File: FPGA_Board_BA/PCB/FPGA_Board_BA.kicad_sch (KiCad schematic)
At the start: 4 parts

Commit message: lots of work
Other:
- note added: "- DCDC for Differential-amplifier [X] ADC power supply (1.8V ... 2.5V) - Breakout for all unused pins - ESD Diode Array for unused pins [X] Add another ADC for B6 [X] CHB Rx En Err -> 10 pin (wie base board) - Poti an Analog Input - ADC Datenbatt Recherche LVDS/CMOS ob 24pin + 2pins für comversion start frei sind [X] FPGA falsche pin namen an Hersteller + BA [X] Level shifter für Tx Rx und Fault 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"
- note removed: "- DCDC for Differential-amplifier [X] ADC power supply (1.8V ... 2.5V) - Breakout for all unused pins - ESD Diode Array for unused pins [X] Add another ADC for B6 - CHB Rx En Err -> 10 pin (wie base board) - Poti an Analog Input - ADC Datenbatt Recherche LVDS/CMOS ob 24pin + 2pins für comversion start frei sind [X] FPGA falsche pin namen an Hersteller + BA - Level shifter für Tx Rx und Fault pins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"
- moved on the sheet: R1, R101, R2, R3

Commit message: work
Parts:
- renumbered R101 to R4
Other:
- sheet ADC for B6 ports: added CNV; removed ~{CNV}
- sheet ADC for Machine ports: added CNV_1; removed ~{CNV}_1
- sheet FPGA ports: added CNV, CNV_1; removed ~{CNV}, ~{CNV}_1
- note added: "- DCDC for Differential-amplifier [X] ADC power supply (1.8V ... 2.5V) - Breakout for all unused pins - ESD Diode Array for unused pins [X] Add another ADC for B6 [X] CHB Rx En Err -> 10 pin (wie base board) [X] Poti an Analog Input - ADC Datenbatt Recherche LVDS/CMOS ob 24pin + 2pins für comversion start frei sind [X] FPGA falsche pin namen an Hersteller + BA [X] Level shifter für Tx Rx und Faul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"
- note removed: "- DCDC for Differential-amplifier [X] ADC power supply (1.8V ... 2.5V) - Breakout for all unused pins - ESD Diode Array for unused pins [X] Add another ADC for B6 [X] CHB Rx En Err -> 10 pin (wie base board) - Poti an Analog Input - ADC Datenbatt Recherche LVDS/CMOS ob 24pin + 2pins für comversion start frei sind [X] FPGA falsche pin namen an Hersteller + BA [X] Level shifter für Tx Rx und Fault 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"
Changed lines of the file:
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@@
 	(generator_version "9.0")
 	(paper "A3")
-	(text "- DCDC for Differential-amplifier\n[X] ADC power supply (1.8V ... 2.5V)\n- Breakout for all unused pins\n- ESD Diode Array for unused pins\n[X] Add another ADC for B6\n[X] CHB Rx En Err -> 10 pin (wie base board)\n- Poti an Analog Input\n- ADC Datenbatt Recherche LVDS/CMOS ob 24pin + 2pins für comversion start frei sind\n[X] FPGA falsche pin namen an Hersteller + BA \n[X] Level shifter für Tx Rx und Fault pins (CHB -> FPGA)\n- Pullup Resistor für Tx der CHB und auch Rx\n[X] Latex dokumentation beginnen\n[X] Diff Eingang für ADC (mit OP-Amps)\n[X] CMOS Fest, DDR mit 2 Widerstände\n[X] HV-Probe hinzufügen\n[X] 26 pin wannenstecker\n- RapidHarness Verkabelung"
+	(text "- DCDC for Differential-amplifier\n[X] ADC power supply (1.8V ... 2.5V)\n- Breakout for all unused pins\n- ESD Diode Array for unused pins\n[X] Add another ADC for B6\n[X] CHB Rx En Err -> 10 pin (wie base board)\n[X] Poti an Analog Input\n- ADC Datenbatt Recherche LVDS/CMOS ob 24pin + 2pins für comversion start frei sind\n[X] FPGA falsche pin namen an Hersteller + BA \n[X] Level shifter für Tx Rx und Fault pins (CHB -> FPGA)\n[X] Pullup Resistor für Tx der CHB und auch Rx\n[X] Latex dokumentation beginnen\n[X] Diff Eingang für ADC (mit OP-Amps)\n[X] CMOS Fest, DDR mit 2 Widerstände\n[X] HV-Probe hinzufügen\n[X] 26 pin wannenstecker\n- RapidHarness Verkabelung\n- 0402 R und C\n- CHB to PCB connect gleich wie beim Base-Board"
 		(exclude_from_sim no)
 		(at 302.26 230.378 0)
@@
 	(wire
 		(pts
-			(xy 115.57 62.23) (xy 156.21 62.23)
+			(xy 115.57 73.66) (xy 156.21 73.66)
 		)
 		(stroke
@@
 	(wire
 		(pts
-			(xy 198.12 72.39) (xy 222.25 72.39)
+			(xy 198.12 95.25) (xy 222.25 95.25)
 		)
 		(stroke
@@
 	(wire
 		(pts
-			(xy 198.12 86.36) (xy 222.25 86.36)
+			(xy 198.12 109.22) (xy 222.25 109.22)
 		)
 		(stroke
@@
 	(wire
 		(pts
-			(xy 115.57 67.31) (xy 156.21 67.31)
+			(xy 115.57 78.74) (xy 156.21 78.74)
 		)
 		(stroke
@@
 	(wire
 		(pts
-			(xy 198.12 67.31) (xy 222.25 67.31)
+			(xy 198.12 90.17) (xy 222.25 90.17)
 		)
 		(stroke
@@
 	(wire
 		(pts
-			(xy 198.12 81.28) (xy 222.25 81.28)
+			(xy 198.12 104.14) (xy 222.25 104.14)
 		)
 		(stroke
@@
 	(wire
 		(pts
-			(xy 198.12 78.74) (xy 222.25 78.74)
+			(xy 198.12 101.6) (xy 222.25 101.6)
 		)
 		(stroke
@@
 	(wire
 		(pts
-			(xy 198.12 96.52) (xy 222.25 96.52)
+			(xy 198.12 119.38) (xy 222.25 119.38)
 		)
 		(stroke
@@
 	(wire
 		(pts
-			(xy 198.12 88.9) (xy 222.25 88.9)
+			(xy 198.12 111.76) (xy 222.25 111.76)
 		)
 		(stroke
@@
 	(wire
 		(pts
-			(xy 115.57 72.39) (xy 156.21 72.39)
+			(xy 115.57 83.82) (xy 156.21 83.82)
 		)
 		(stroke
@@
 	(wire
 		(pts
-			(xy 198.12 91.44) (xy 222.25 91.44)
+			(xy 198.12 114.3) (xy 222.25 114.3)
 		)
 		(stroke
@@
 	(wire
 		(pts
-			(xy 198.12 83.82) (xy 222.25 83.82)
+			(xy 198.12 106.68) (xy 222.25 106.68)
 		)
 		(stroke
@@
 	(wire
 		(pts
-			(xy 198.12 69.85) (xy 222.25 69.85)
+			(xy 198.12 92.71) (xy 222.25 92.71)
 		)
 		(stroke
@@
 	(wire
 		(pts
-			(xy 198.12 93.98) (xy 222.25 93.98)
+			(xy 198.12 116.84) (xy 222.25 116.84)
 		)
 		(stroke
@@
 	(wire
 		(pts
-			(xy 115.57 64.77) (xy 156.21 64.77)
+			(xy 115.57 76.2) (xy 156.21 76.2)
 		)
 		(stroke
@@
 	(wire
 		(pts
-			(xy 115.57 69.85) (xy 156.21 69.85)
+			(xy 115.57 81.28) (xy 156.21 81.28)
 		)
 		(stroke
@@
 		(on_board yes)
 		(dnp no)
-		(property "Reference" "R101"
+		(property "Reference" "R4"
 			(at 360.426 80.518 90)
 			(effects
@@
 			(project "FPGA_Board_BA"
 				(path "/fd7503bc-e7fc-4766-b224-3d1c3d7de5ff"
-					(reference "R101")
+					(reference "R4")
 					(unit 1)
 				)
@@
 	)
 	(sheet
-		(at 90.17 59.69)
+		(at 90.17 71.12)
 		(size 25.4 15.24)
 		(exclude_from_sim no)
@@
 		)
 		(property "Sheetname" "User Interaction"
-			(at 90.17 58.9784 0)
+			(at 90.17 70.4084 0)
 			(effects
 				(font
@@
 		)
 		(property "Sheetfile" "user_interaction.kicad_sch"
-			(at 90.17 75.5146 0)
+			(at 90.17 86.9446 0)
 			(effects
 				(font
@@
 		)
 		(pin "Button1" output
-			(at 115.57 62.23 0)
+			(at 115.57 73.66 0)
 			(effects
 				(font
@@
 		)
 		(pin "Button2" output
-			(at 115.57 64.77 0)
+			(at 115.57 76.2 0)
 			(effects
 				(font
@@
 		)
 		(pin "LED1" input
-			(at 115.57 67.31 0)
+			(at 115.57 78.74 0)
 			(effects
 				(font
@@
 		)
 		(pin "LED2" input
-			(at 115.57 69.85 0)
+			(at 115.57 81.28 0)
 			(effects
 				(font
@@
 		)
 		(pin "Poti" output
-			(at 115.57 72.39 0)
+			(at 115.57 83.82 0)
 			(effects
 				(font
@@
 	)
 	(sheet
-		(at 222.25 59.69)
-		(size 34.29 83.82)
+		(at 222.25 69.85)
+		(size 34.29 73.66)
 		(exclude_from_sim no)
 		(in_bom yes)
@@
 		)
 		(property "Sheetname" "ADC for Machine"
-			(at 222.25 58.9784 0)
+			(at 222.25 69.1384 0)
 			(effects
 				(font
@@
 		)
 		(pin "CLK_IN_1" input
-			(at 222.25 67.31 180)
+			(at 222.25 90.17 180)
 			(effects
 				(font
@@
 		)
 		(pin "CLK_OUT_1" input
-			(at 222.25 69.85 180)
+			(at 222.25 92.71 180)
 			(effects
 				(font
@@
 		)
 		(pin "SDO1_1" output
-			(at 222.25 78.74 180)
+			(at 222.25 101.6 180)
 			(effects
 				(font
@@
 		)
 		(pin "SDO2_1" output
-			(at 222.25 81.28 180)
+			(at 222.25 104.14 180)
 			(effects
 				(font
@@
 		)
 		(pin "SDO3_1" output
-			(at 222.25 83.82 180)
+			(at 222.25 106.68 180)
 			(effects
 				(font
@@
 		)
 		(pin "SDO4_1" output
-			(at 222.25 86.36 180)
+			(at 222.25 109.22 180)
 			(effects
 				(font
@@
 		)
 		(pin "SDO5_1" output
-			(at 222.25 88.9 180)
+			(at 222.25 111.76 180)
 			(effects
 				(font
@@
 		)
 		(pin "SDO6_1" output
-			(at 222.25 91.44 180)
+			(at 222.25 114.3 180)
 			(effects
 				(font
@@
 		)
 		(pin "SDO7_1" output
-			(at 222.25 93.98 180)
+			(at 222.25 116.84 180)
 			(effects
 				(font
@@
 		)
 		(pin "SDO8_1" output
-			(at 222.25 96.52 180)
+			(at 222.25 119.38 180)
 			(effects
 				(font
@@
 			)
 		)
-		(pin "~{CNV}_1" input
-			(at 222.25 72.39 180)
+		(pin "CNV_1" input
+			(at 222.25 95.25 180)
 			(effects
 				(font
@@
 	)
 	(sheet
-		(at 156.21 58.42)
-		(size 41.91 220.98)
+		(at 156.21 64.77)
+		(size 41.91 214.63)
 		(exclude_from_sim no)
 		(in_bom yes)
@@
 		)
 		(property "Sheetname" "FPGA"
-			(at 156.21 57.7084 0)
+			(at 156.21 64.0584 0)
 			(effects
 				(font
@@
 			)
 		)
-		(pin "~{CNV}" output
-			(at 198.12 180.34 0)
-			(effects
-				(font
-					(size 1.27 1.27)
-				)
-				(justify right)
-			)
-		)
 		(pin "Ph_C_Tx1" input
 			(at 156.21 181.61 180)
@@
 		)
 		(pin "Button1" input
-			(at 156.21 62.23 180)
+			(at 156.21 73.66 180)
 			(effects
 				(font
@@
 		)
 		(pin "Button2" input
-			(at 156.21 64.77 180)
+			(at 156.21 76.2 180)
 			(effects
 				(font
@@
 		)
 		(pin "LED1" output
-			(at 156.21 67.31 180)
+			(at 156.21 78.74 180)
 			(effects
 				(font
@@
 		)
 		(pin "LED2" output
-			(at 156.21 69.85 180)
+			(at 156.21 81.28 180)
 			(effects
 				(font
@@
 		)
 		(pin "Poti" input
-			(at 156.21 72.39 180)
+			(at 156.21 83.82 180)
 			(effects
 				(font
@@
 		)
 		(pin "CLK_IN_1" output
-			(at 198.12 67.31 0)
+			(at 198.12 90.17 0)
 			(effects
 				(font
@@
 		)
 		(pin "CLK_OUT_1" output
-			(at 198.12 69.85 0)
+			(at 198.12 92.71 0)
 			(effects
 				(font
@@
 		)
 		(pin "SDO1_1" input
-			(at 198.12 78.74 0)
+			(at 198.12 101.6 0)
 			(effects
 				(font
@@
 		)
 		(pin "SDO2_1" input
-			(at 198.12 81.28 0)
+			(at 198.12 104.14 0)
 			(effects
 				(font
@@
 		)
 		(pin "SDO3_1" input
-			(at 198.12 83.82 0)
+			(at 198.12 106.68 0)
 			(effects
 				(font
@@
 		)
 		(pin "SDO4_1" input
-			(at 198.12 86.36 0)
+			(at 198.12 109.22 0)
 			(effects
 				(font
@@
 		)
 		(pin "SDO5_1" input
-			(at 198.12 88.9 0)
+			(at 198.12 111.76 0)
 			(effects
 				(font
@@
 		)
 		(pin "SDO6_1" input
-			(at 198.12 91.44 0)
+			(at 198.12 114.3 0)
 			(effects
 				(font
@@
 		)
 		(pin "SDO7_1" input
-			(at 198.12 93.98 0)
+			(at 198.12 116.84 0)
 			(effects
 				(font
@@
 		)
 		(pin "SDO8_1" input
-			(at 198.12 96.52 0)
+			(at 198.12 119.38 0)
 			(effects
 				(font
@@
 			)
 		)
-		(pin "~{CNV}_1" output
-			(at 198.12 72.39 0)
+		(pin "CNV_1" output
+			(at 198.12 95.25 0)
+			(effects
+				(font
+					(size 1.27 1.27)
+				)
+				(justify right)
+			)
+		)
+		(pin "CNV" output
+			(at 198.12 180.34 0)
 			(effects
 				(font
@@
 			)
 		)
-		(pin "~{CNV}" input
-			(at 223.52 180.34 180)
-			(effects
-				(font
-					(size 1.27 1.27)
-				)
-				(justify left)
-			)
-		)
 		(pin "I_A" input
 			(at 232.41 213.36 270)
@@
 			(effects
 				(font
+					(size 1.27 1.27)
+				)
+				(justify left)
+			)
+		)
+		(pin "CNV" input
+			(at 223.52 180.34 180)
+			(effects
+				(font

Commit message: 18.11 Bib Session
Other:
- sheet ADC for B6 ports: added ~{CNV}; removed CNV
- sheet ADC for Machine ports: added ~{CNV}_1; removed CNV_1
- sheet FPGA ports: added ~{CNV}, ~{CNV}_1; removed CNV, CNV_1
- note added: "- DCDC for Isolation-amplifier [X] ADC power supply (1.8V ... 2.5V) - Breakout for all unused pins - ESD Diode Array for unused pins [X] Add another ADC for B6 [X] CHB Rx En Err -> 10 pin (wie base board) [X] Poti an Analog Input [X] ADC Datenbatt Recherche LVDS/CMOS ob 24pin + 2pins für comversion start frei sind [X] FPGA falsche pin namen an Hersteller + BA [X] Level shifter für Tx Rx und Fault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"
- note removed: "- DCDC for Differential-amplifier [X] ADC power supply (1.8V ... 2.5V) - Breakout for all unused pins - ESD Diode Array for unused pins [X] Add another ADC for B6 [X] CHB Rx En Err -> 10 pin (wie base board) [X] Poti an Analog Input - ADC Datenbatt Recherche LVDS/CMOS ob 24pin + 2pins für comversion start frei sind [X] FPGA falsche pin namen an Hersteller + BA [X] Level shifter für Tx Rx und Faul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"
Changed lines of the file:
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@@
 	(generator_version "9.0")
 	(paper "A3")
-	(text "- DCDC for Differential-amplifier\n[X] ADC power supply (1.8V ... 2.5V)\n- Breakout for all unused pins\n- ESD Diode Array for unused pins\n[X] Add another ADC for B6\n[X] CHB Rx En Err -> 10 pin (wie base board)\n[X] Poti an Analog Input\n- ADC Datenbatt Recherche LVDS/CMOS ob 24pin + 2pins für comversion start frei sind\n[X] FPGA falsche pin namen an Hersteller + BA \n[X] Level shifter für Tx Rx und Fault pins (CHB -> FPGA)\n[X] Pullup Resistor für Tx der CHB und auch Rx\n[X] Latex dokumentation beginnen\n[X] Diff Eingang für ADC (mit OP-Amps)\n[X] CMOS Fest, DDR mit 2 Widerstände\n[X] HV-Probe hinzufügen\n[X] 26 pin wannenstecker\n- RapidHarness Verkabelung\n- 0402 R und C\n- CHB to PCB connect gleich wie beim Base-Board"
+	(text "- DCDC for Isolation-amplifier\n[X] ADC power supply (1.8V ... 2.5V)\n- Breakout for all unused pins\n- ESD Diode Array for unused pins\n[X] Add another ADC for B6\n[X] CHB Rx En Err -> 10 pin (wie base board)\n[X] Poti an Analog Input\n[X] ADC Datenbatt Recherche LVDS/CMOS ob 24pin + 2pins für comversion start frei sind\n[X] FPGA falsche pin namen an Hersteller + BA \n[X] Level shifter für Tx Rx und Fault pins (CHB -> FPGA)\n[X] Pullup Resistor für Tx der CHB und auch Rx\n[X] Latex dokumentation beginnen\n[X] Diff Eingang für ADC (mit OP-Amps)\n[X] CMOS Fest, DDR mit 2 Widerstände\n[X] HV-Probe hinzufügen\n[X] 26 pin wannenstecker\n- CHB to PCB Connector \n- 0402 R und C (maybe)\n- Plug Terminal 8 Pin Footprint korrigieren\n- Alle unconnected pins mit dem \"not-connected\" funktion machen"
 		(exclude_from_sim no)
 		(at 302.26 230.378 0)
@@
 			)
 		)
-		(pin "CLK_OUT_1" input
-			(at 222.25 92.71 180)
-			(effects
-				(font
-					(size 1.27 1.27)
-				)
-				(justify left)
-			)
-		)
 		(pin "SDO1_1" output
 			(at 222.25 101.6 180)
@@
 			)
 		)
-		(pin "CNV_1" input
-			(at 222.25 95.25 180)
-			(effects
-				(font
-					(size 1.27 1.27)
-				)
-				(justify left)
-			)
-		)
 		(pin "Vout_1" input
 			(at 256.54 121.92 0)
@@
 			)
 		)
+		(pin "CLK_OUT_1" output
+			(at 222.25 92.71 180)
+			(effects
+				(font
+					(size 1.27 1.27)
+				)
+				(justify left)
+			)
+		)
+		(pin "~{CNV}_1" input
+			(at 222.25 95.25 180)
+			(effects
+				(font
+					(size 1.27 1.27)
+				)
+				(justify left)
+			)
+		)
 		(instances
 			(project "FPGA_Board_BA"
@@
 			)
 		)
-		(pin "CLK_OUT" output
-			(at 198.12 177.8 0)
-			(effects
-				(font
-					(size 1.27 1.27)
-				)
-				(justify right)
-			)
-		)
 		(pin "Ph_C_Tx1" input
 			(at 156.21 181.61 180)
@@
 			)
 		)
-		(pin "CLK_OUT_1" output
-			(at 198.12 92.71 0)
-			(effects
-				(font
-					(size 1.27 1.27)
-				)
-				(justify right)
-			)
-		)
 		(pin "SDO1_1" input
 			(at 198.12 101.6 0)
@@
 			)
 		)
-		(pin "CNV_1" output
-			(at 198.12 95.25 0)
+		(pin "CLK_OUT_1" input
+			(at 198.12 92.71 0)
 			(effects
 				(font
@@
 			)
 		)
-		(pin "CNV" output
+		(pin "CLK_OUT" input
+			(at 198.12 177.8 0)
+			(effects
+				(font
+					(size 1.27 1.27)
+				)
+				(justify right)
+			)
+		)
+		(pin "~{CNV}" output
 			(at 198.12 180.34 0)
 			(effects
@@
 			)
 		)
+		(pin "~{CNV}_1" output
+			(at 198.12 95.25 0)
+			(effects
+				(font
+					(size 1.27 1.27)
+				)
+				(justify right)
+			)
+		)
 		(instances
 			(project "FPGA_Board_BA"
@@
 			)
 		)
-		(pin "CLK_OUT" input
-			(at 223.52 177.8 180)
-			(effects
-				(font
-					(size 1.27 1.27)
-				)
-				(justify left)
-			)
-		)
 		(pin "SDO1" output
 			(at 223.52 185.42 180)
@@
 			)
 		)
-		(pin "CNV" input
+		(pin "CLK_OUT" output
+			(at 223.52 177.8 180)
+			(effects
+				(font
+					(size 1.27 1.27)
+				)
+				(justify left)
+			)
+		)
+		(pin "~{CNV}" input
 			(at 223.52 180.34 180)
 			(effects

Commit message: Besprechung mit Leo
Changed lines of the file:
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@@
 	(generator_version "9.0")
 	(paper "A3")
-	(text "- DCDC for Isolation-amplifier\n[X] ADC power supply (1.8V ... 2.5V)\n- Breakout for all unused pins\n- ESD Diode Array for unused pins\n[X] Add another ADC for B6\n[X] CHB Rx En Err -> 10 pin (wie base board)\n[X] Poti an Analog Input\n[X] ADC Datenbatt Recherche LVDS/CMOS ob 24pin + 2pins für comversion start frei sind\n[X] FPGA falsche pin namen an Hersteller + BA \n[X] Level shifter für Tx Rx und Fault pins (CHB -> FPGA)\n[X] Pullup Resistor für Tx der CHB und auch Rx\n[X] Latex dokumentation beginnen\n[X] Diff Eingang für ADC (mit OP-Amps)\n[X] CMOS Fest, DDR mit 2 Widerstände\n[X] HV-Probe hinzufügen\n[X] 26 pin wannenstecker\n- CHB to PCB Connector \n- 0402 R und C (maybe)\n- Plug Terminal 8 Pin Footprint korrigieren\n- Alle unconnected pins mit dem \"not-connected\" funktion machen"
+	(text "- DCDC for Isolation-amplifier\n[X] ADC power supply (1.8V ... 2.5V)\n- Breakout for all unused pins\n- ESD Diode Array for unused pins\n[X] Add another ADC for B6\n[X] CHB Rx En Err -> 10 pin (wie base board)\n[X] Poti an Analog Input\n[X] ADC Datenbatt Recherche LVDS/CMOS ob 24pin + 2pins für comversion start frei sind\n[X] FPGA falsche pin namen an Hersteller + BA \n[X] Level shifter für Tx Rx und Fault pins (CHB -> FPGA)\n[X] Pullup Resistor für Tx der CHB und auch Rx\n[X] Latex dokumentation beginnen\n[X] Diff Eingang für ADC (mit OP-Amps)\n[X] CMOS Fest, DDR mit 2 Widerstände\n[X] HV-Probe hinzufügen\n[X] 26 pin wannenstecker\n- CHB to PCB Connector \n- 0402 R und C (maybe)\n- Plug Terminal 8 Pin Footprint korrigieren\n- Alle unconnected pins mit dem \"not-connected\" funktion machen\n- Drehzahlsensor widerstand zum dir pin von level shifter\n- En Pulldown (wahrscheinlich (muss noch nachschauen))\n- Error auch\n- Rx vor dem Level-Shifter pull-up\n- Leo link schicken über 24 pin Wannenstecker Mouser\n- Noch einen Poti \n- Refout -> 2 Opamps für diff-Eingang (Vref/2)\n- Xilinx pinout anschauen + Versorgung\n- Vllt ein Bank auf 1.8V"
 		(exclude_from_sim no)
-		(at 302.26 230.378 0)
+		(at 278.892 244.348 0)
 		(effects
 			(font

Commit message: 22.11
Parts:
- removed R1, R2, R3, R4: 0R100_2512, Resistor_SMD:R_2512_6332Metric_Pad1.40x3.35mm_HandSolder, symbol MYLIB_R:0R100_2512
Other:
- removed sheet ADC power
- sheet ADC for Machine ports: added Iin_1, Iin_2, Iin_3, Iin_4; removed none
- sheet Current measure ports: added PHA, PHB, PHC, PHD; removed PHA_OUTN, PHA_OUTP, PHB_OUTN, PHB_OUTP, PHC_OUTN, PHC_OUTP, PHD_OUTN, PHD_OUTP
- sheet FPGA ports: added LED3, Poti2; removed none
- sheet User Interaction ports: added LED3, Poti2; removed none
- note added: "[X] Breakout for all unused pins - ESD Diode Array for unused pins [X] CHB to PCB Connector - 0402 R und C (maybe) - Alle unconnected pins mit dem "not-connected" funktion machen [X] Drehzahlsensor widerstand zum dir pin von level shifter [X] En Pulldown (wahrscheinlich (muss noch nachschauen)) [X] Error auch [X] Rx vor dem Level-Shifter pull-up [X] Leo link schicken über 24 pin Wannenstecker Mou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"
- note removed: "- DCDC for Isolation-amplifier [X] ADC power supply (1.8V ... 2.5V) - Breakout for all unused pins - ESD Diode Array for unused pins [X] Add another ADC for B6 [X] CHB Rx En Err -> 10 pin (wie base board) [X] Poti an Analog Input [X] ADC Datenbatt Recherche LVDS/CMOS ob 24pin + 2pins für comversion start frei sind [X] FPGA falsche pin namen an Hersteller + BA [X] Level shifter für Tx Rx und Fault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"

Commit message: exported stuff
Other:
- sheet Power from CHB ports: added PH_A1, PH_C1, PH_D1; removed Ph_A1, Ph_C1, Ph_D1
- note removed: "[X] Breakout for all unused pins - ESD Diode Array for unused pins [X] CHB to PCB Connector - 0402 R und C (maybe) - Alle unconnected pins mit dem "not-connected" funktion machen [X] Drehzahlsensor widerstand zum dir pin von level shifter [X] En Pulldown (wahrscheinlich (muss noch nachschauen)) [X] Error auch [X] Rx vor dem Level-Shifter pull-up [X] Leo link schicken über 24 pin Wannenstecker Mou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"
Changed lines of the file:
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@@
 	(generator_version "9.0")
 	(paper "A3")
-	(text "[X] Breakout for all unused pins\n- ESD Diode Array for unused pins\n[X] CHB to PCB Connector \n- 0402 R und C (maybe)\n- Alle unconnected pins mit dem \"not-connected\" funktion machen\n[X] Drehzahlsensor widerstand zum dir pin von level shifter\n[X] En Pulldown (wahrscheinlich (muss noch nachschauen))\n[X] Error auch\n[X] Rx vor dem Level-Shifter pull-up\n[X] Leo link schicken über 24 pin Wannenstecker Mouser\n[X] Noch einen Poti \n[X] Refout -> 2 Opamps für diff-Eingang (Vref/2)\n[X] Xilinx pinout anschauen + Versorgung\n[X] Tamura Hall-Sensor hinzufügen\n- Add 4 pin TVS diode array"
-		(exclude_from_sim no)
-		(at 278.638 230.632 0)
-		(effects
-			(font
-				(size 1.27 1.27)
-			)
-			(justify left)
-		)
-	)
 	(junction
 		(at 368.3 135.89)
@@
 			)
 		)
-		(pin "Ph_A1" output
+		(pin "PH_A1" output
 			(at 332.74 36.83 270)
 			(effects
@@
 			)
 		)
-		(pin "Ph_C1" output
+		(pin "PH_C1" output
 			(at 353.06 36.83 270)
 			(effects
@@
 			)
 		)
-		(pin "Ph_D1" output
+		(pin "PH_D1" output
 			(at 363.22 36.83 270)
 			(effects

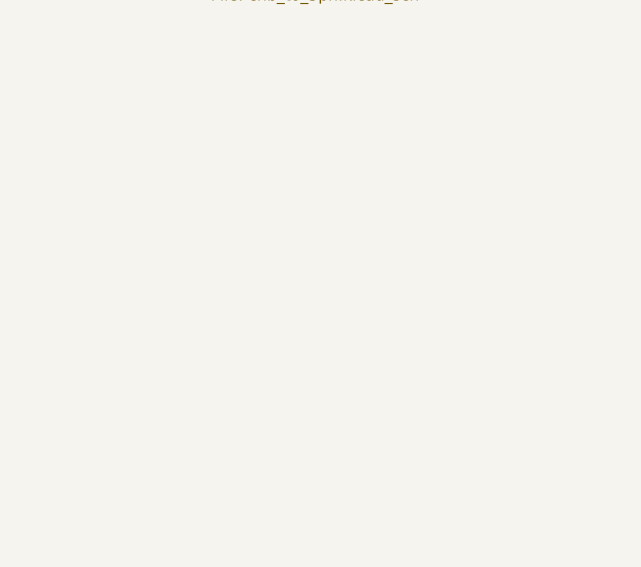
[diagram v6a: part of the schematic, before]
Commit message: added Wannenstecker 24pin + BOM
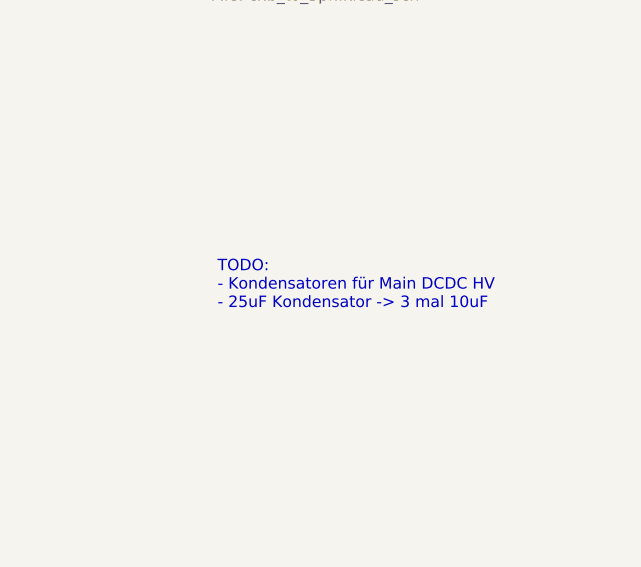
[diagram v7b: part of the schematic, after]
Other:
- note added: "TODO: - Kondensatoren für Main DCDC HV - 25uF Kondensator -> 3 mal 10uF"
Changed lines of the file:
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@@
 	(generator_version "9.0")
 	(paper "A3")
+	(text "TODO:\n- Kondensatoren für Main DCDC HV\n- 25uF Kondensator -> 3 mal 10uF "
+		(exclude_from_sim no)
+		(at 328.422 239.268 0)
+		(effects
+			(font
+				(size 1.27 1.27)
+			)
+			(justify left)
+		)
+	)
 	(junction
 		(at 368.3 135.89)
